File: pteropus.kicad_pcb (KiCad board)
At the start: 2 copper layers, 284 x 139 mm, 100 parts, among them J1 USB_C_Receptacle_USB2.0, SW1 B3FS-1002P, SW10 SW_SPST, SW11 SW_SPST, SW12 SW_SPST, SW13 SW_SPST, SW14 SW_SPST, SW15 SW_SPST, SW16 SW_SPST, SW17 SW_SPST, SW18 SW_SPST, SW19 SW_SPST, SW2 B3FS-1002P, SW20 SW_SPST, SW21 SW_SPST, SW22 SW_SPST, SW23 SW_SPST, SW24 SW_SPST, SW25 SW_SPST, SW26 SW_SPST, SW27 SW_SPST, SW28 SW_SPST, SW29 SW_SPST, SW3 SW_SPST, SW30 SW_SPST, SW31 SW_SPST, SW32 SW_SPST, SW33 SW_SPST, SW34 SW_SPST, SW35 SW_SPST, SW36 SW_SPST, SW37 SW_SPST, SW38 SW_SPST, SW4 SW_SPST, SW5 SW_SPST, SW6 SW_SPST, SW7 SW_SPST, SW8 SW_SPST, SW9 SW_SPST, U1 MCP1700x-330xxTT, U2 USBLC6-2SC6, U3 STM32F072C8Tx

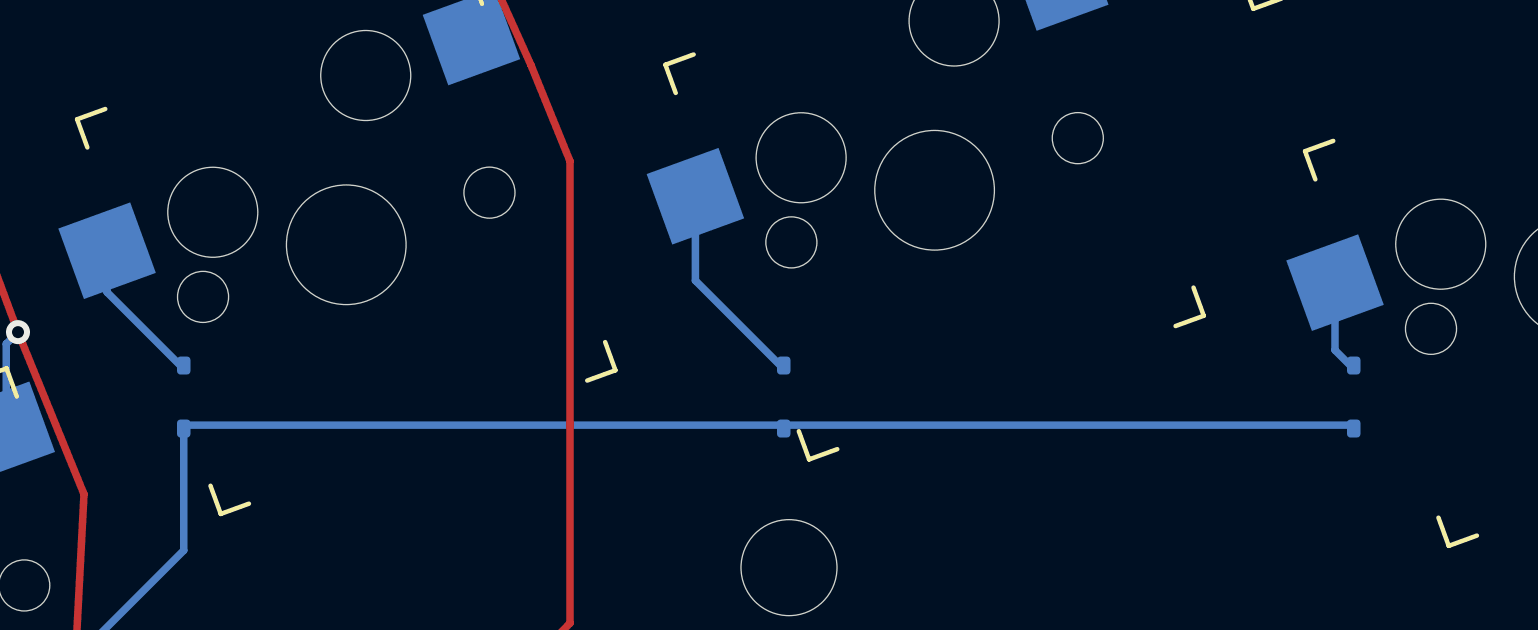
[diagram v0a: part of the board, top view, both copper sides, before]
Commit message: Relocate D29 diode.
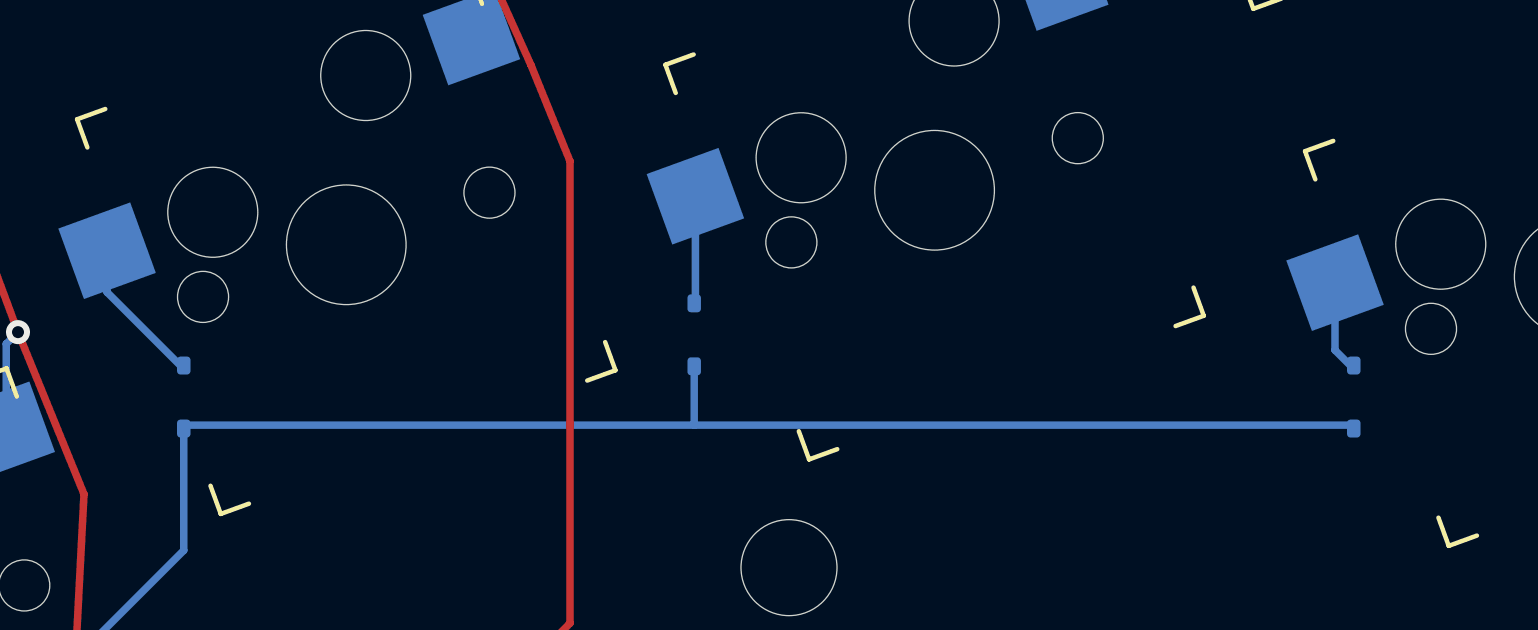
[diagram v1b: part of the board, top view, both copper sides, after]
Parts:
- moved D29 3.63 mm to (96.8, 37.2)
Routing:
- net Net-(D29-A): track 6.97 -> 3.59 mm
- net Row:3: track 332.6 -> 334.6 mm
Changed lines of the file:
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@@
   )
   (footprint "Diode_SMD:D_SOD-323" (layer "B.Cu")
-    (at 99.825 39.3125 90)
+    (at 96.84 37.24 90)
     (descr "SOD-323")
     (tags "SOD-323")
@@
   (segment (start 62.325 54.1875) (end 70.0625 54.1875) (width 0.25) (layer "B.Cu") (net 31))
   (segment (start -58.152379 61.05) (end -59.8 59.9) (width 0.25) (layer "B.Cu") (net 31))
+  (segment (start 79.825 40.25) (end 96.84 40.25) (width 0.25) (layer "B.Cu") (net 31))
   (segment (start -22.7 23.05) (end -33.7 34.05) (width 0.25) (layer "B.Cu") (net 31))
   (segment (start 25.4 28.45) (end 25.4 38.7125) (width 0.25) (layer "B.Cu") (net 31))
   (segment (start -33.7 47.35) (end -47.4 61.05) (width 0.25) (layer "B.Cu") (net 31))
   (segment (start -77.1 49.9) (end -88.15 38.65) (width 0.25) (layer "B.Cu") (net 31))
-  (segment (start 79.825 40.25) (end 118.825 40.25) (width 0.25) (layer "B.Cu") (net 31))
   (segment (start 41 54.3125) (end 41.5625 53.75) (width 0.25) (layer "B.Cu") (net 31))
   (segment (start -47.4 61.05) (end -58.152379 61.05) (width 0.25) (layer "B.Cu") (net 31))
   (segment (start 60.6 53.75) (end 61.0375 54.1875) (width 0.25) (layer "B.Cu") (net 31))
   (segment (start -72.925 49.625) (end -77.1 49.9) (width 0.25) (layer "B.Cu") (net 31))
+  (segment (start 96.84 40.25) (end 96.84 38.29) (width 0.25) (layer "B.Cu") (net 31))
   (segment (start -14.986744 15.336744) (end -6.485048 15.336744) (width 0.25) (layer "B.Cu") (net 31))
   (segment (start -90.661613 38.782863) (end -133.088387 38.782863) (width 0.25) (layer "B.Cu") (net 31))
@@
   (segment (start 70.0625 54.1875) (end 79.825 44.425) (width 0.25) (layer "B.Cu") (net 31))
   (segment (start -59.8 59.9) (end -62.8625 59.6875) (width 0.25) (layer "B.Cu") (net 31))
+  (segment (start 96.84 40.25) (end 118.825 40.25) (width 0.25) (layer "B.Cu") (net 31))
   (segment (start -88.15 38.65) (end -88.6675 38.65) (width 0.25) (layer "B.Cu") (net 31))
   (segment (start -59.266345 57.378845) (end -59.8 57.8) (width 0.25) (layer "B.Cu") (net 32))
@@
   (segment (start 77.269193 34.436853) (end 77.269193 35.819193) (width 0.25) (layer "B.Cu") (net 35))
   (segment (start 77.269193 35.819193) (end 79.825 38.375) (width 0.25) (layer "B.Cu") (net 35))
-  (segment (start 96.880193 35.430193) (end 99.825 38.375) (width 0.25) (layer "B.Cu") (net 36))
-  (segment (start 96.880193 32.619853) (end 96.880193 35.430193) (width 0.25) (layer "B.Cu") (net 36))
+  (segment (start 96.880193 36.149807) (end 96.84 36.19) (width 0.25) (layer "B.Cu") (net 36))
+  (segment (start 96.880193 32.619853) (end 96.880193 36.149807) (width 0.25) (layer "B.Cu") (net 36))
   (segment (start 118.201193 35.500853) (end 118.201193 37.751193) (width 0.25) (layer "B.Cu") (net 37))
   (segment (start 118.201193 37.751193) (end 118.825 38.375) (width 0.25) (layer "B.Cu") (net 37))
